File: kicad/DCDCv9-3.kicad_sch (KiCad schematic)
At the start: 188 parts, among them J1 Screw_Terminal_01x03, J1.1 Screw_Terminal_01x03, J1.2 Screw_Terminal_01x03, J2 Conn_01x02_Male, J3 Conn_01x02, J3.1 Conn_01x02, J3.2 Conn_01x01_Pin, J3.3 Conn_01x01_Pin, J4 Conn_01x02_Male, J5 XT60 Male, J5.1 XT60 Female (wrong symbol ik), J6 Conn_01x02_Male, J7 Conn_01x02_Male, J8 Conn_01x02_Male, M1 Fan, Q1 PMV20ENR, Q10 IMBG65R050M2HXTMA1, Q11 IMBG65R050M2HXTMA1, Q2 PMV20ENR, Q3 SIHP24N80AE-GE3, Q4 IXYP8N90C3, Q5 PMV20ENR, Q6 PMV20ENR, Q7 PMV20ENR, T1 DIY Transformer ETD 39, T1.1 Ferrite Core, T1.2 Ferrite Core (gapped), T1.3 1800 mm 120 x 0.1 mm HF litz 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, T1.4 165 mm 600 x 0,071 mm HF litz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, T1.5 165 mm 600 x 0,071 mm HF litz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, U1 TBA 1-1212HI, U10 LM2904BIDDFR, U11 UCC21520DW, U12 UCC25600, U13 ZXRE330ASA-7, U14 LM2904BIDDFR, U2 RT9058-90GVL, U3 MP4541_SOP8-EP, U4 TLV61048DBVR, U6 LM2904BIDDFR, U7 TL431, U9 ACPL-217-50AE

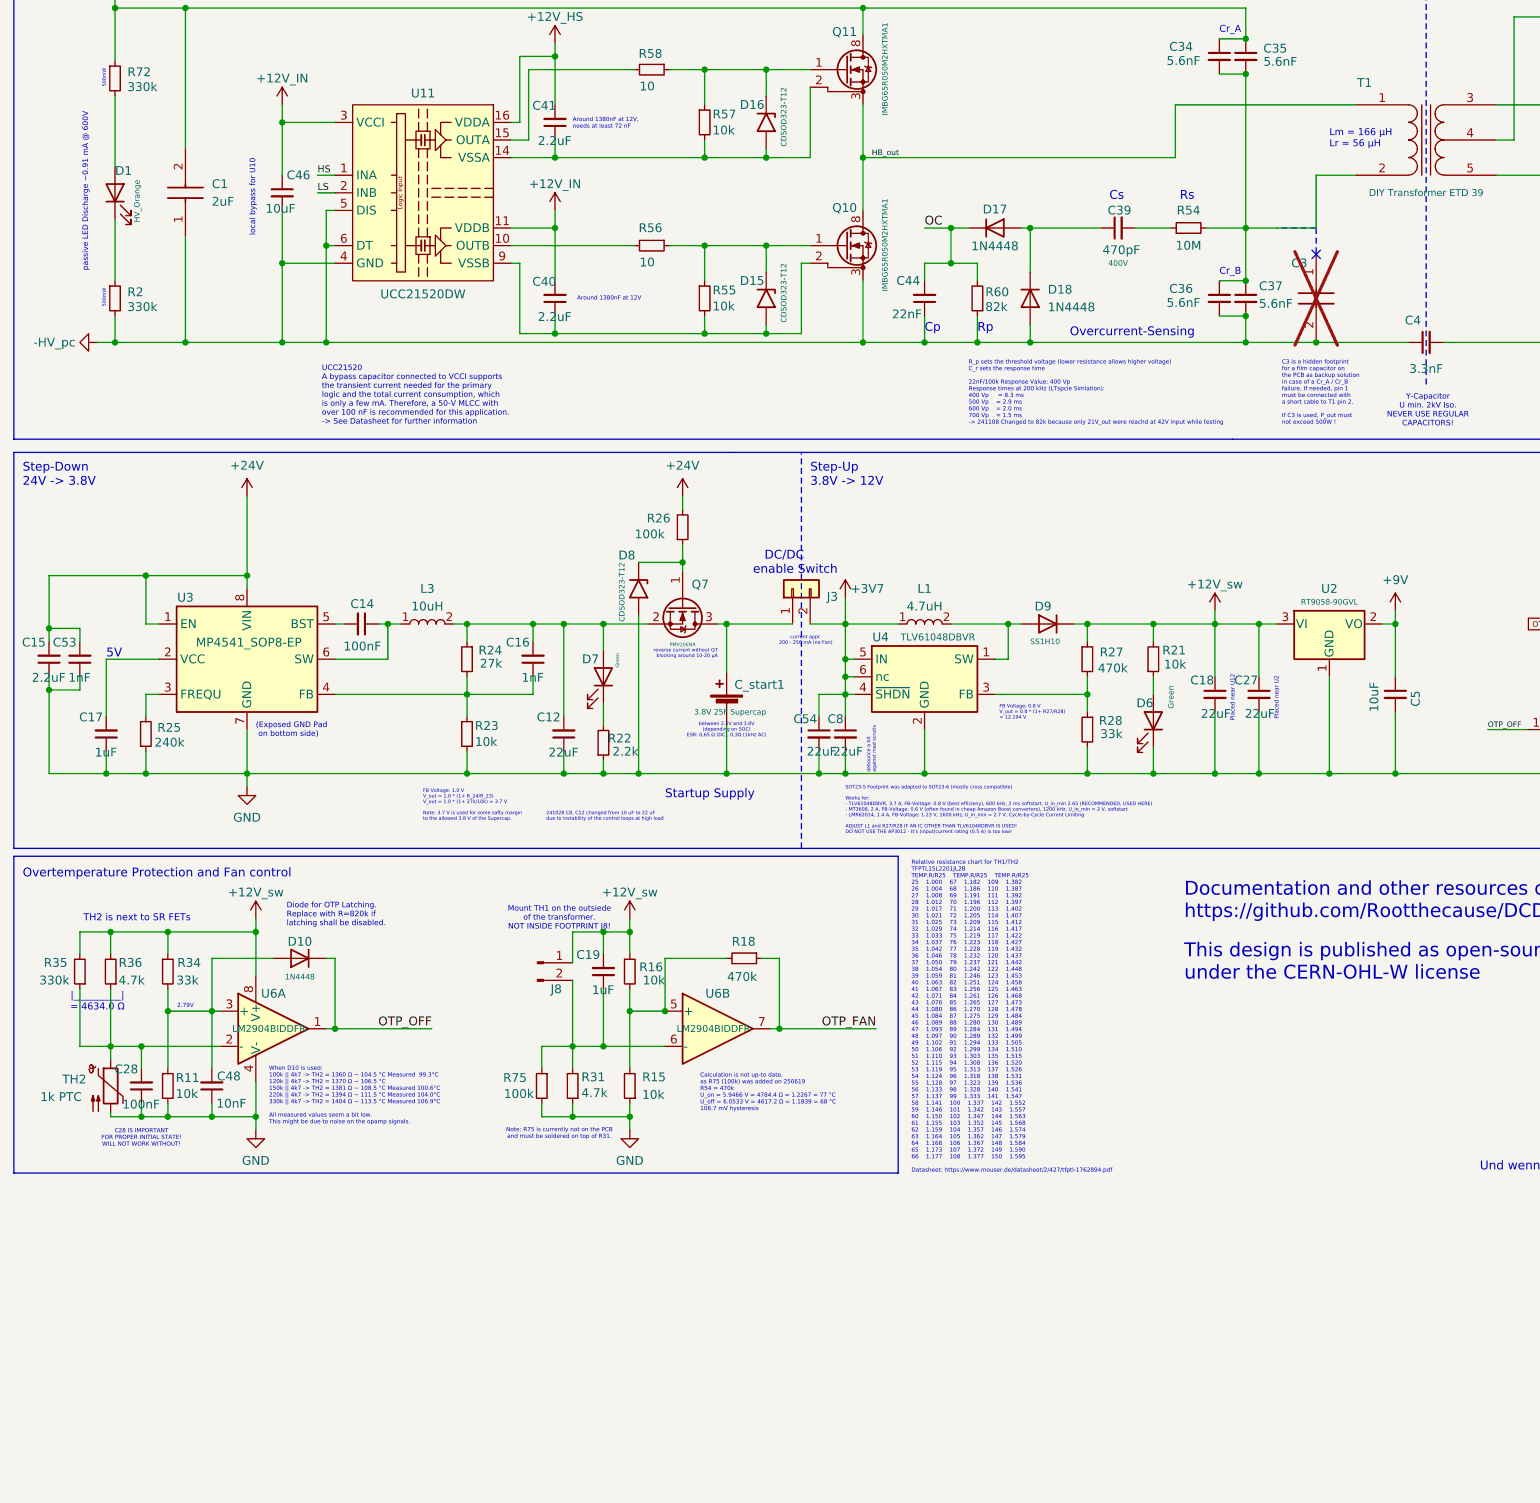
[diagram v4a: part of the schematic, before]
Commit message: fixed typo in schematic and README
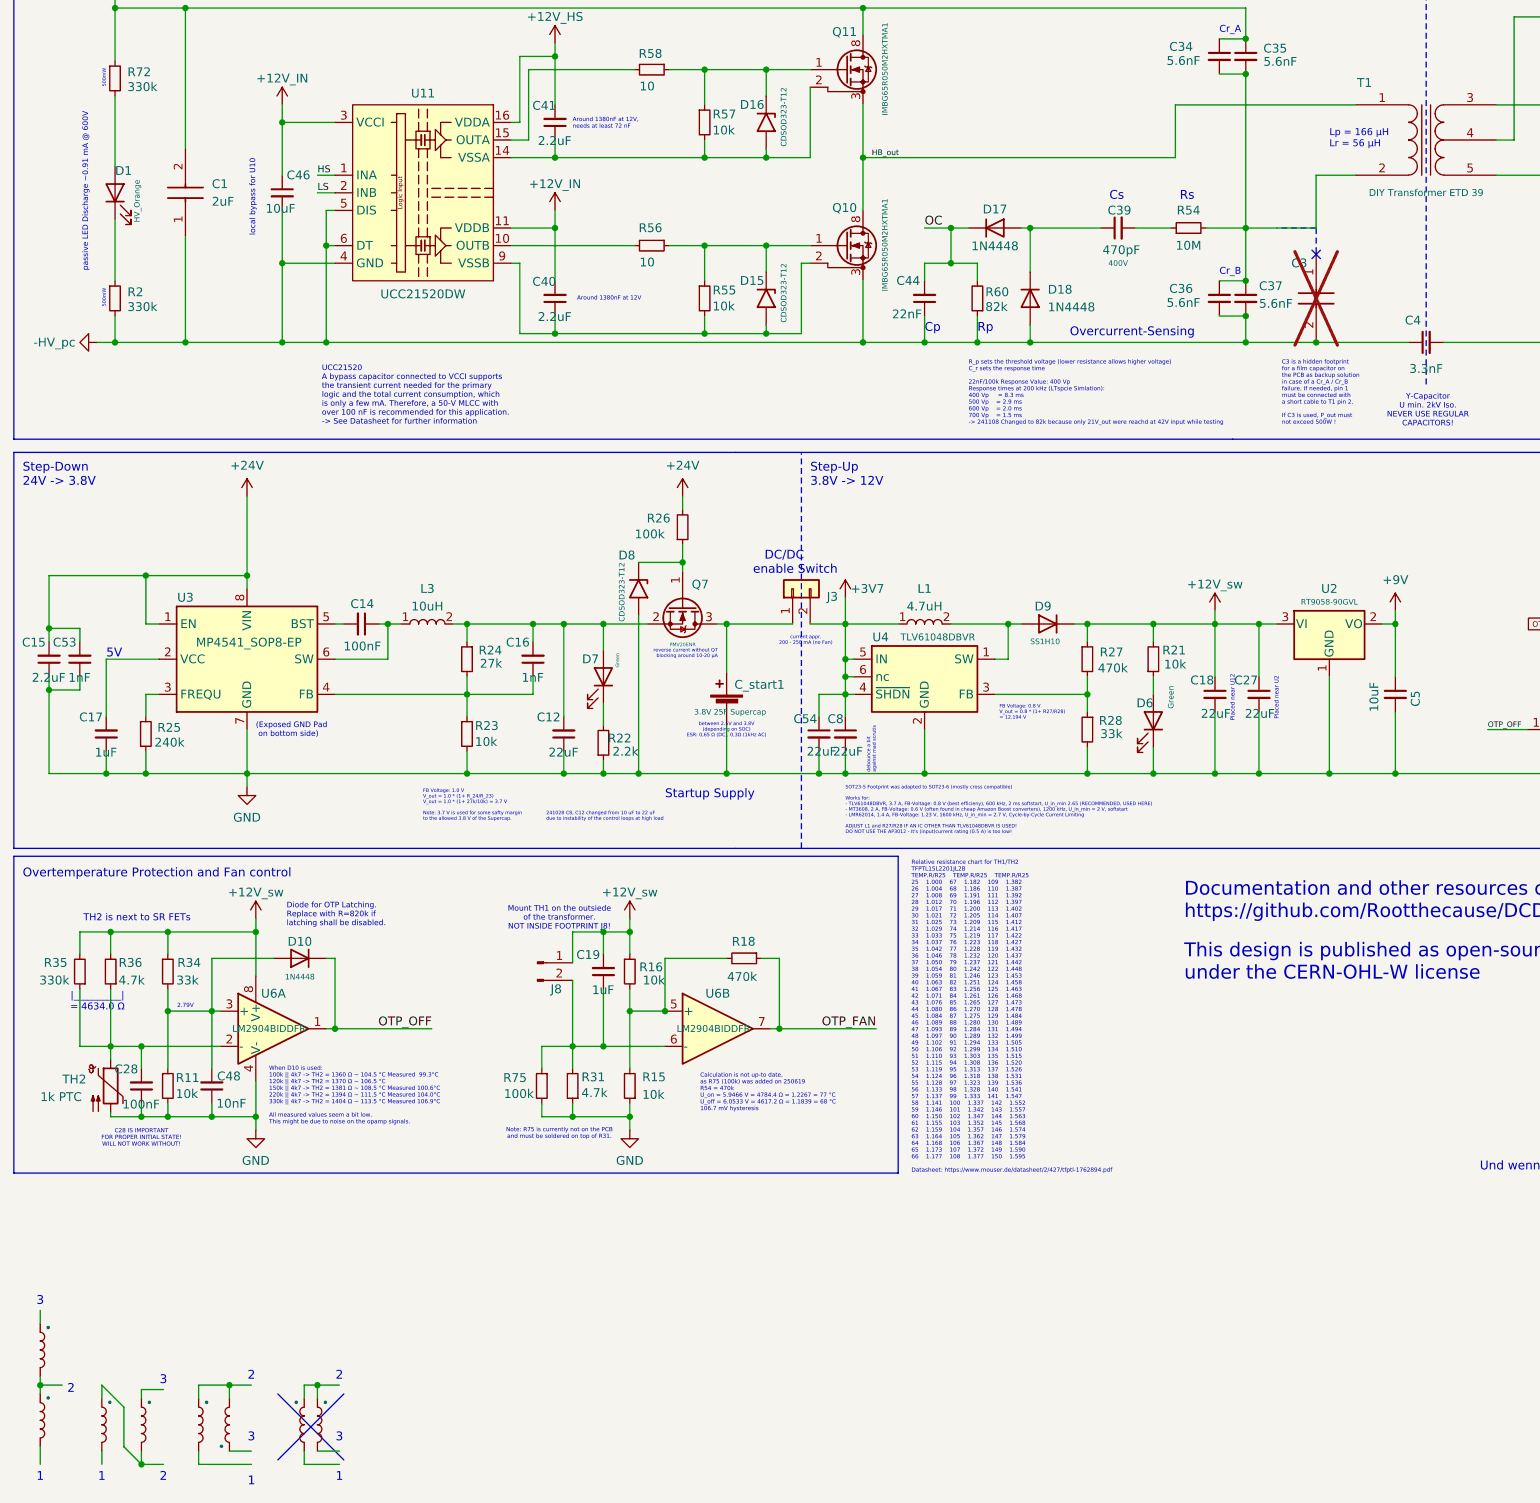
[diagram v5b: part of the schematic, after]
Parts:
- added L10, L11, L4, L5, L6, L7, L8, L9: •, symbol Device:L
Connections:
- new net: L8.1, L9.1
- new net: L10.1, L11.2
- new net: L6.1, L7.2
- new net: L4.2, L5.1
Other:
- note added: "1"
- note added: "2"
- note added: "3"
- note added: "Lp = 166 µH Lr = 56 µH"
- note removed: "Lm = 166 µH Lr = 56 µH"

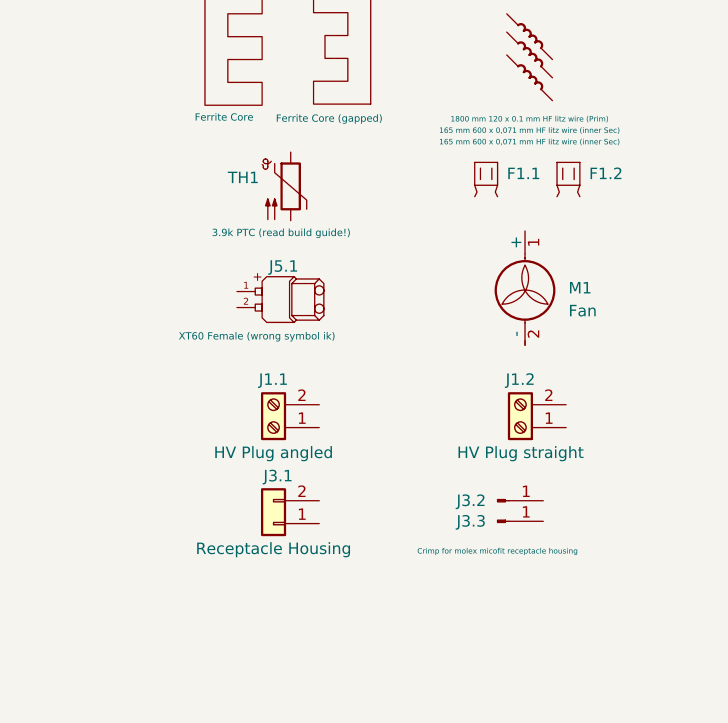
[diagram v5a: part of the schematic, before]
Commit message: updated build notes, added primary winding video
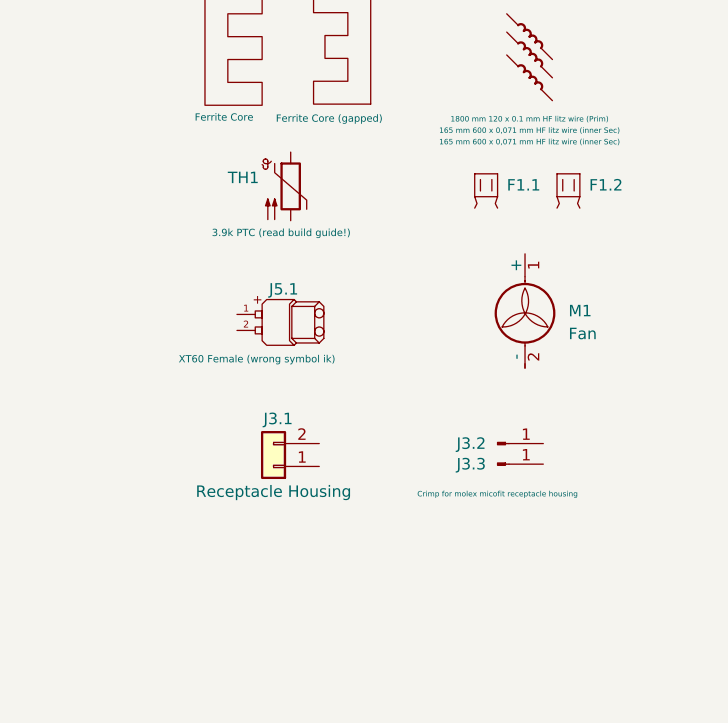
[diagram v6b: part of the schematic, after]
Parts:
- removed J1.1, J1.2: Screw_Terminal_01x03, ~, symbol Connector:Screw_Terminal_01x02
- J1: Manufacturer_Part_Number 282828-2 -> 691416600002
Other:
- moved on the sheet: F1.1, F1.2, J3.1, J3.2, J3.3, J5.1, M1

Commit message: large DCDCv9-3r1.4 release update
- Removed some tables in csv and ods format (xlsx preferred)
- fixed issue #10 (waiting for approval)
- added video of adhesive testing for ESG10C-20G
- added video of primary and secondary winding
- updated all documentation files incl. Scrutineering Support Presentation
- updated transformer isolator part
- updated build notes
- updated README.md
- updated HV input connector
- added note about the discontinuation of the German versions
- added R75 onto the PCB (not required to solder on top of R31 anymore)
- updated iBoms and comments
- removed solder mask between TS an LV for better inspection
- replaced J1, unified crimps for all molex housings
- replaced U1
- fresh production files and gerber PDF plots
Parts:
- removed J1: Screw_Terminal_01x03, DCDC-Footprints:TerminalBlock_TE-282817-2_1x03_P5.00mm_90 Degrees updated v9-3, symbol Connector:Screw_Terminal_01x02
- added J1: 43650-0315, Samacsys:43650-03YY_151617, symbol Samacsys:43650-0315
- added J1.1: 43645-0300, symbol Samacsys:43650-0315
- added J1.2, J1.3, J1.4: Conn_01x01_Pin, ~, symbol Connector:Conn_01x01_Pin
- C12, C14, C15, C16, C17, C18, C19, C2, C20, C21, C22, C23, C24, C26, C27, C28, C29, C3, C30, C32, C33, C38, C39, C40, C41, C42, C43, C44, C45, C46, C47, C48, C49, C5, C50, C51, C52, C53, C54, C55, C56, C57, C8, D1, D10, D13, D15, D16, D17, D18, D2, D3, D4, D5, D6, D7, D8, D9, J6, J7, Q1, Q2, Q5, Q6, Q7, R1, R10, R11, R12, R15, R16, R17, R18, R2, R21, R22, R23, R24, R25, R26, R27, R28, R3, R31, R34, R35, R36, R37, R39, R4, R41, R44, R45, R46, R47, R48, R49, R5, R50, R51, R52, R53, R54, R55, R56, R57, R58, R59, R6, R60, R61, R62, R63, R64, R65, R66, R67, R68, R69, R7, R70, R71, R72, R73, R74, R8, R9, U10, U11, U12, U14, U4, U6, U7, U9: ignore for iBOM 1 -> (none); ignore for iBOM PCBA (none) -> 1
- J3.2, J3.3: Manufacturer_Part_Number 35044-9102 -> 43030-0039
- R75: ignore for iBOM PCBA (none) -> 1
- RV1: comment set dead time, R3 can be used for a fixed value. Should be 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 -> set dead time, R3 can be used for a fixed value. Read Build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
- RV2: comment used to set minimum switching freqeuncy, should be adjusted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 -> Used to set minimum switching frequency. Read Build guide c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
- T1: comment see Documentation chapter "Transformer" -> Read Build guide chapter 5 for more info.
- U1: value TBA 1-1212HI -> RP-1515S; Manufacturer_Part_Number TBA 1-1212HI -> RP-1515S; comment If not available, use PD01S1212A https://www.mouser.de/Prod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 -> (none)
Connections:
- net +HV_in: now also J1.3
- net -HV_in: now also J1.1
- no-connect marks 1 -> 34
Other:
- note added: "Crimp for molex micofit"
- note removed: "Note: R75 is currently not on the PCB and must be soldered on top of R31."
- title: DC/DC v9-3r1 -> DC/DC v9-3r1.4

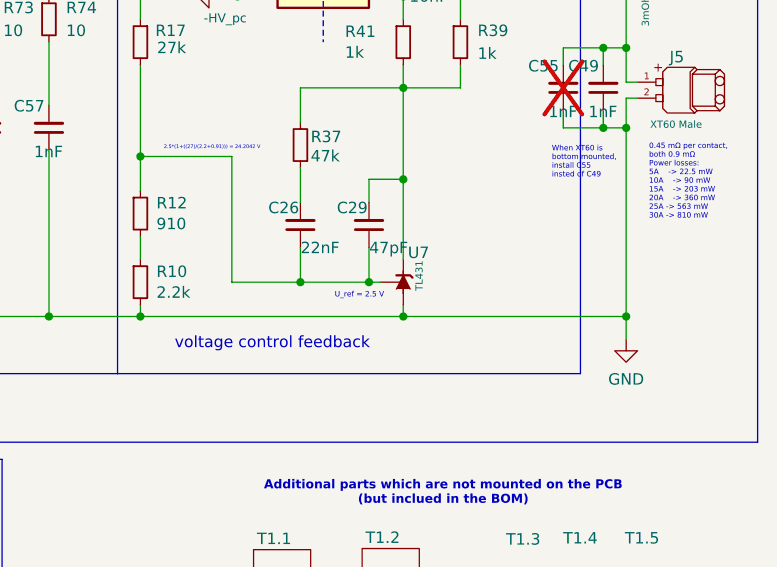
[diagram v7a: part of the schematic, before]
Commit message: Fixed TL431 LCSC part number, added single winding holder for 12V version
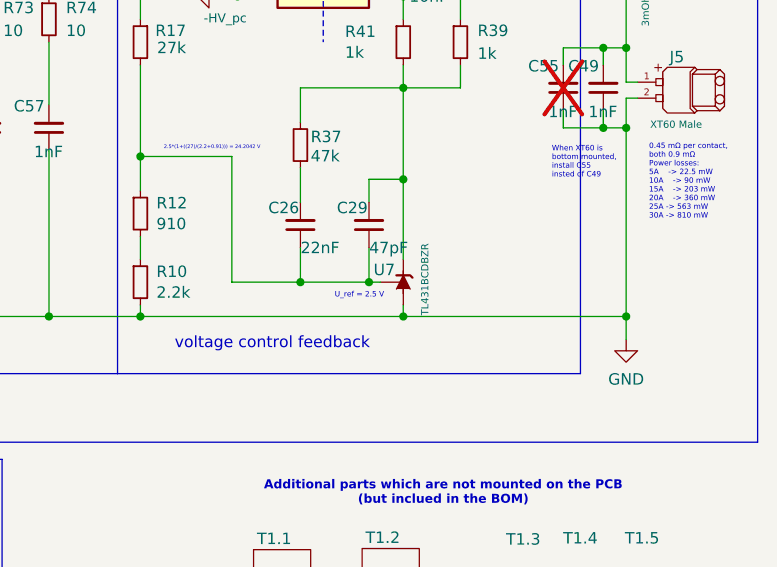
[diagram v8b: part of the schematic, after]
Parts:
- U7: value TL431 -> TL431BCDBZR
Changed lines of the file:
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@@
 		(dnp no)
 		(property "Reference" "U7"
-			(at 366.903 156.7434 90)
+			(at 363.093 158.6484 90)
 			(effects
 				(font
@@
 			)
 		)
-		(property "Value" "TL431"
-			(at 368.173 157.607 0)
+		(property "Value" "TL431BCDBZR"
+			(at 368.808 155.702 0)
 			(effects
 				(font
